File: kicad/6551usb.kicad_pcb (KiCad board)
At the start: 2 copper layers, 98.6 x 139.7 mm, 42 parts, among them J1 Conn_01x03_Male, P1 DLP-USB245R, SW1 SW_DIP_x06, U1 74LS04, U10 74LS74, U11 74LS86, U12 74LS33, U13 74LS273, U14 74LS374, U15 74LS244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

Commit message: Update to 1.01
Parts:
- U7: value 74LS09 -> 74LS08; footprint Package_DIP:DIP-20_W7.62mm -> Package_DIP:DIP-14_W7.62mm
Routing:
- net /D4: track 257.1 -> 203.1 mm, vias 2 -> 1
- net GND: track 700.5 -> 647.5 mm, vias 0 -> 1
- net /D0: track 244.6 -> 191.7 mm, vias 1 -> 2
- net /D6: track 250.3 -> 201.3 mm, vias 1 -> 2
- net /BUF_WRITE: track 118.3 -> 79.4 mm, vias 0 -> 1
- net /D3: track 231.2 -> 265.6 mm, vias 2 -> 1
- net /A6: track 136.1 -> 102.5 mm
- net /DELTA_PWREN*: track 66.9 -> 92.2 mm, vias 1 -> 0
- net /CD1: track 98.4 -> 79.2 mm, vias 1 -> 0
- net /COMMAND_SELECT: track 61.2 -> 42.6 mm
- net /D1: track 201.5 -> 219.5 mm, vias 2 -> 1
- net +5V: track 467.3 -> 451.8 mm
- net /A7: track 141.3 -> 125.9 mm, vias 0 -> 1
- net /CONTROL_SELECT: track 78.7 -> 63.4 mm
- net /A0: track 113.8 -> 99.9 mm
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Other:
- board text added: "USB Serial Pak for Color Computer v1.01 Copyright 2022 Don Barber License GPLv3 https://github.com/barberd/cocousbserial"
- board text removed: "USB Serial Pak for Color Computer v1.0 Copyright 2022 Don Barber License GPLv3 https://github.com/barberd/cocousbserial"

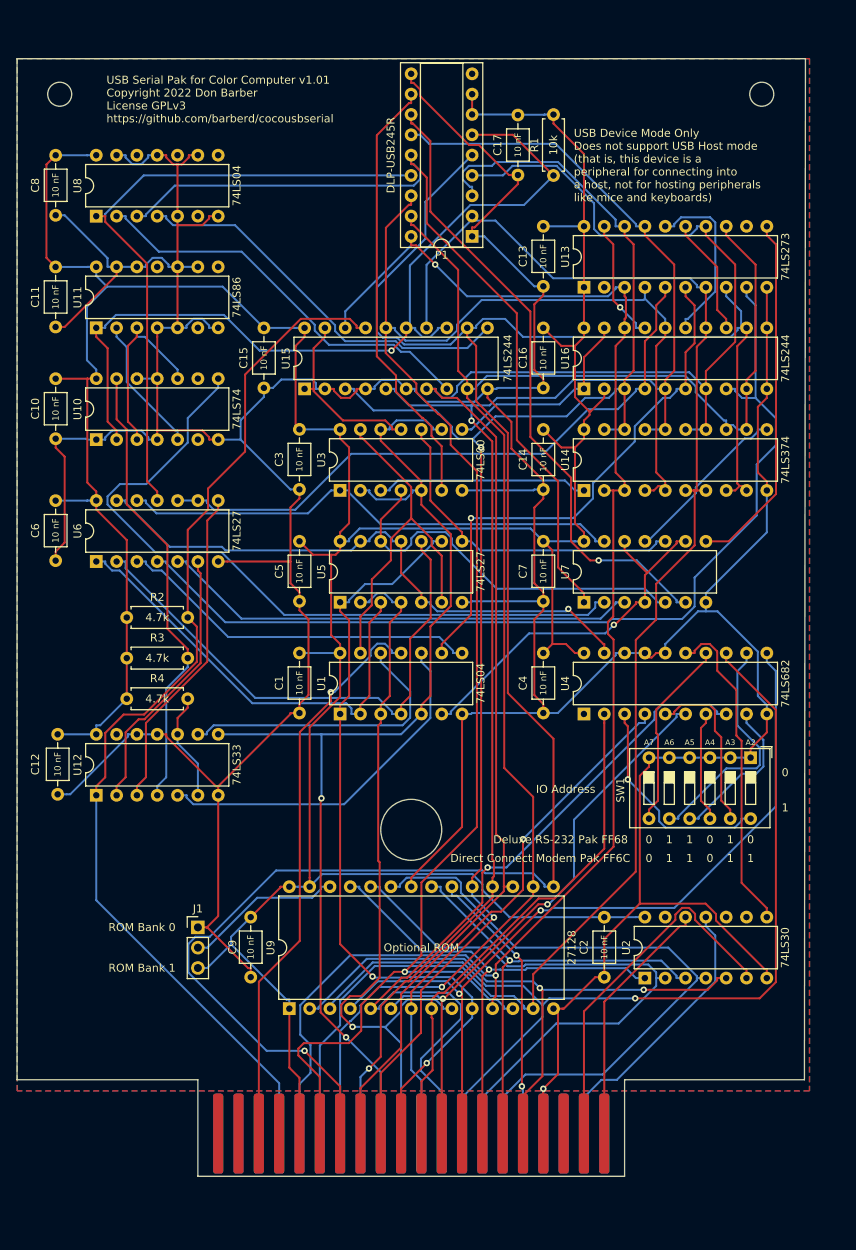
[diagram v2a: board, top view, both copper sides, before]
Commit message: Updated to 1.02 to fix E line
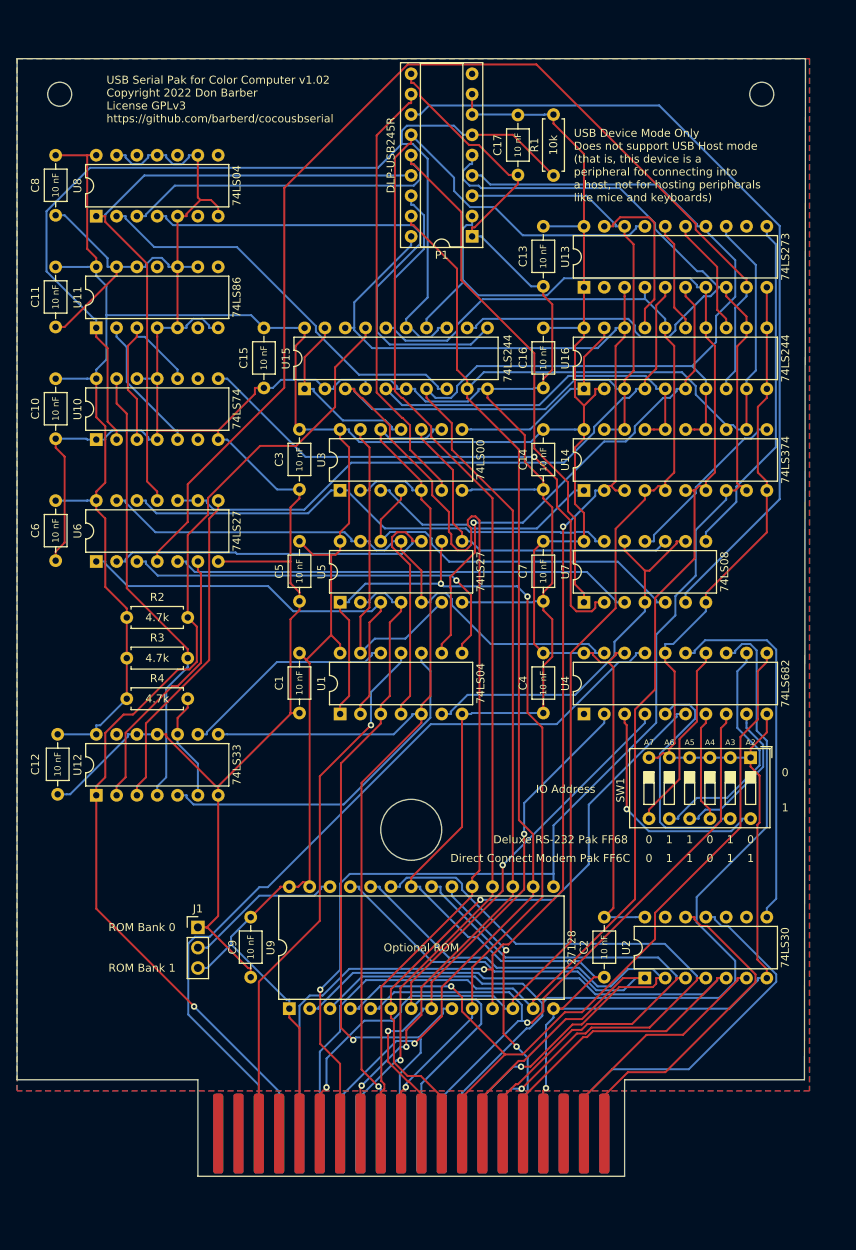
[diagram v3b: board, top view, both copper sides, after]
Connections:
- net /BOARD_SELECT renamed /BOARD_SELECT*
- U17 pad 6: unconnected-(U17-Pad6) -> /E
- U4 pad 17: GND -> /E
- U4 pad 18: GND -> +5V
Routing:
- net /E: track 0.00 -> 99.7 mm
- net /D3: track 265.6 -> 227.9 mm
- net /PWREN*: track 107.2 -> 136.3 mm, vias 1 -> 0
- net /D1: track 219.5 -> 194.0 mm
- net /BUF_WRITE: track 79.4 -> 104.7 mm, vias 1 -> 0
- net /DELTA_PWREN*: track 92.2 -> 69.4 mm, vias 0 -> 1
- net /CD3: track 121.2 -> 143.8 mm
- net /A0: track 99.9 -> 120.7 mm, vias 2 -> 3
- net /D6: track 201.3 -> 221.0 mm, vias 2 -> 1
- net /A12: track 76.5 -> 92.4 mm, vias 2 -> 0
- net /A13: track 46.1 -> 31.2 mm
- net GND: track 647.5 -> 662.4 mm
- net Net-(U15-Pad11): track 49.8 -> 63.9 mm
- net /A14: track 35.5 -> 47.4 mm
- net /A10: track 59.1 -> 70.8 mm, vias 1 -> 0
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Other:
- board text added: "USB Serial Pak for Color Computer v1.02 Copyright 2022 Don Barber License GPLv3 https://github.com/barberd/cocousbserial"
- board text removed: "USB Serial Pak for Color Computer v1.01 Copyright 2022 Don Barber License GPLv3 https://github.com/barberd/cocousbserial"

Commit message: Updated to 1.03 to fix interrupt in status register and extend board to full size
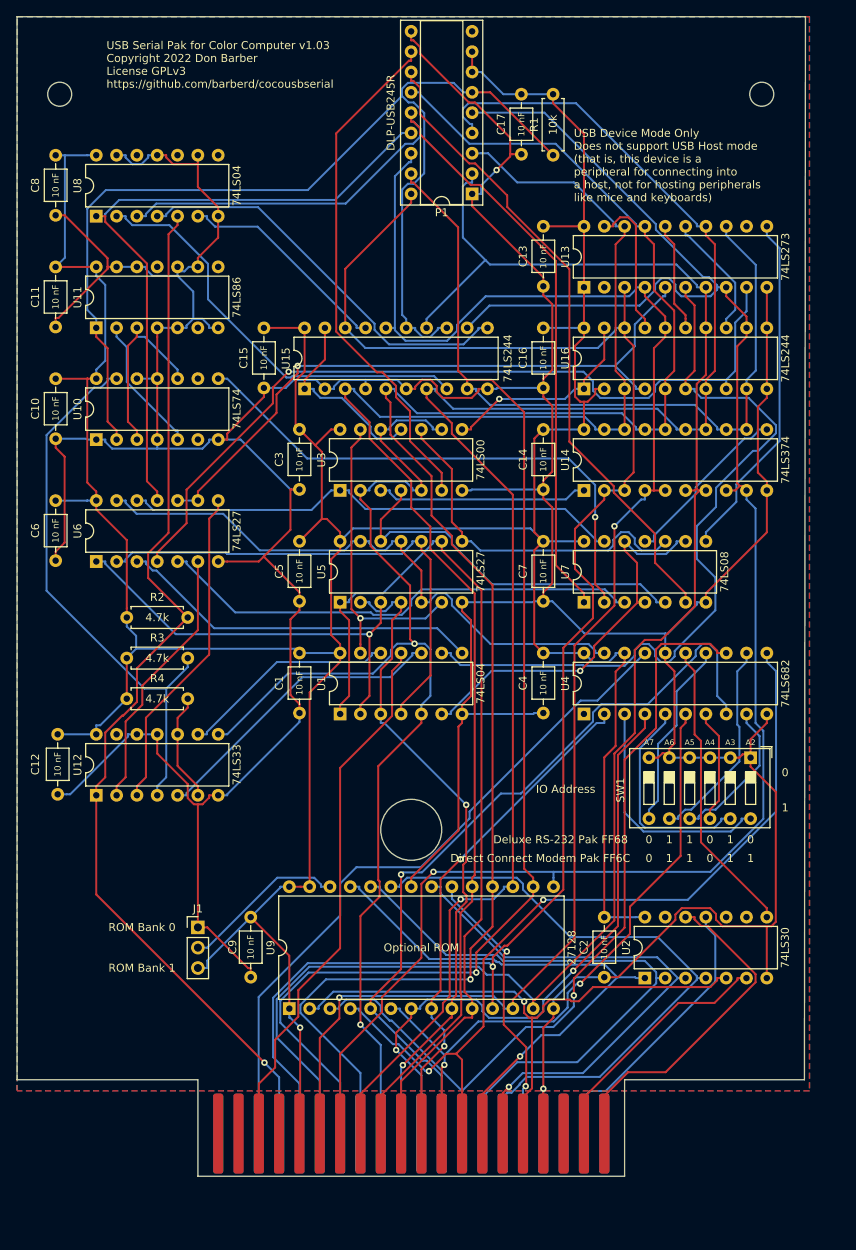
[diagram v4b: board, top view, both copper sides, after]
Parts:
- moved P1 5.31 mm to (69.8, 72.2)
- moved C17 2.64 mm to (76.0, 59.7)
- moved R1 2.54 mm to (80.0, 67.3)
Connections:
- U15 pad 17: /CART* -> /CART
- U8 pad 5: GND -> /CART*
- U8 pad 6: unconnected-(U8-Pad6) -> /CART
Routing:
- net /CD3: track 143.8 -> 102.4 mm, vias 0 -> 1
- net /CD2: track 65.8 -> 96.5 mm, vias 1 -> 0
- net /CART: track 0.00 -> 27.1 mm
- net /BUF_WRITE: track 104.7 -> 81.1 mm
- net /A7: track 127.8 -> 104.5 mm, vias 0 -> 1
- net /D4: track 200.3 -> 222.6 mm
- net /A12: track 92.4 -> 73.0 mm, vias 0 -> 1
- net /D2: track 195.6 -> 212.2 mm
- net /E: track 99.7 -> 86.0 mm
- net Net-(U15-Pad11): track 63.9 -> 50.4 mm
- net Net-(R3-Pad2): track 57.3 -> 70.1 mm
- net /D7: track 203.8 -> 191.4 mm
- net /D0: track 194.4 -> 206.6 mm, vias 2 -> 1
- net /A14: track 47.4 -> 35.5 mm
- net GND: track 662.4 -> 650.5 mm, vias 1 -> 2
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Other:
- board size 98.6 x 139.7 mm -> 98.6 x 144.9 mm
- board text added: "USB Serial Pak for Color Computer v1.03 Copyright 2022 Don Barber License GPLv3 https://github.com/barberd/cocousbserial"
- board text removed: "USB Serial Pak for Color Computer v1.02 Copyright 2022 Don Barber License GPLv3 https://github.com/barberd/cocousbserial"

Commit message: fixed fab files in kicad folder
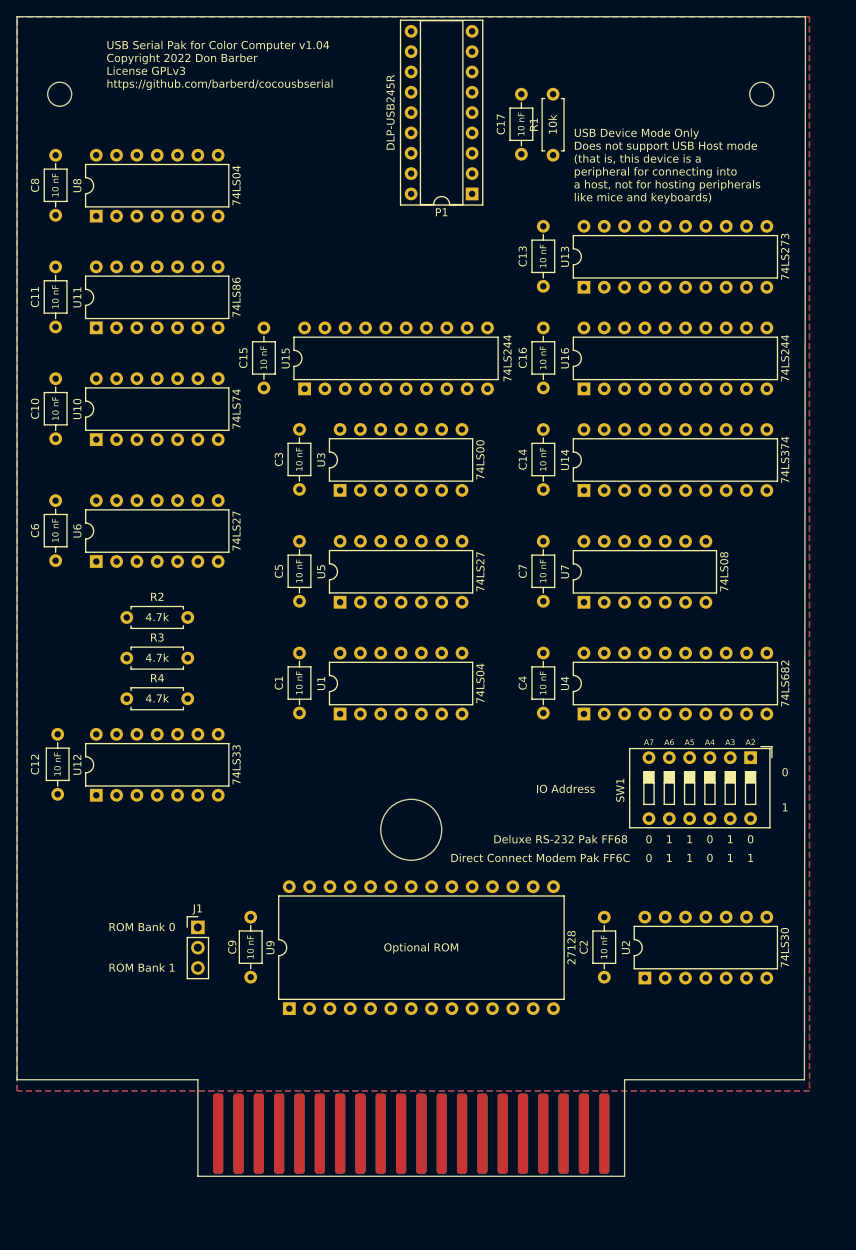
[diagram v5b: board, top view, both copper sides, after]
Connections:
- U10 pad 1: GND -> +5V
- U10 pad 4: GND -> +5V
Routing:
- net GND: track 650.5 -> 0.00 mm, vias 2 -> 0
- net +5V: track 455.9 -> 0.00 mm, vias 1 -> 0
- net /D3: track 232.7 -> 0.00 mm, vias 1 -> 0
- net /D6: track 223.5 -> 0.00 mm, vias 1 -> 0
- net /D4: track 222.6 -> 0.00 mm, vias 1 -> 0
- net /D5: track 213.0 -> 0.00 mm, vias 1 -> 0
- net /D2: track 212.2 -> 0.00 mm
- net /D0: track 206.6 -> 0.00 mm, vias 1 -> 0
- net /D1: track 201.5 -> 0.00 mm, vias 2 -> 0
- net /D7: track 191.4 -> 0.00 mm
- net /R/W*: track 146.7 -> 0.00 mm, vias 2 -> 0
- net /PWREN*: track 138.0 -> 0.00 mm
- net /CART*: track 132.5 -> 0.00 mm, vias 1 -> 0
- net /TXE*: track 114.3 -> 0.00 mm
- net /A0: track 112.7 -> 0.00 mm
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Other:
- board text added: "USB Serial Pak for Color Computer v1.04 Copyright 2022 Don Barber License GPLv3 https://github.com/barberd/cocousbserial"
- board text removed: "USB Serial Pak for Color Computer v1.03 Copyright 2022 Don Barber License GPLv3 https://github.com/barberd/cocousbserial"

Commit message: Updated to 1.04 to fix PWREN flipflop set and reset
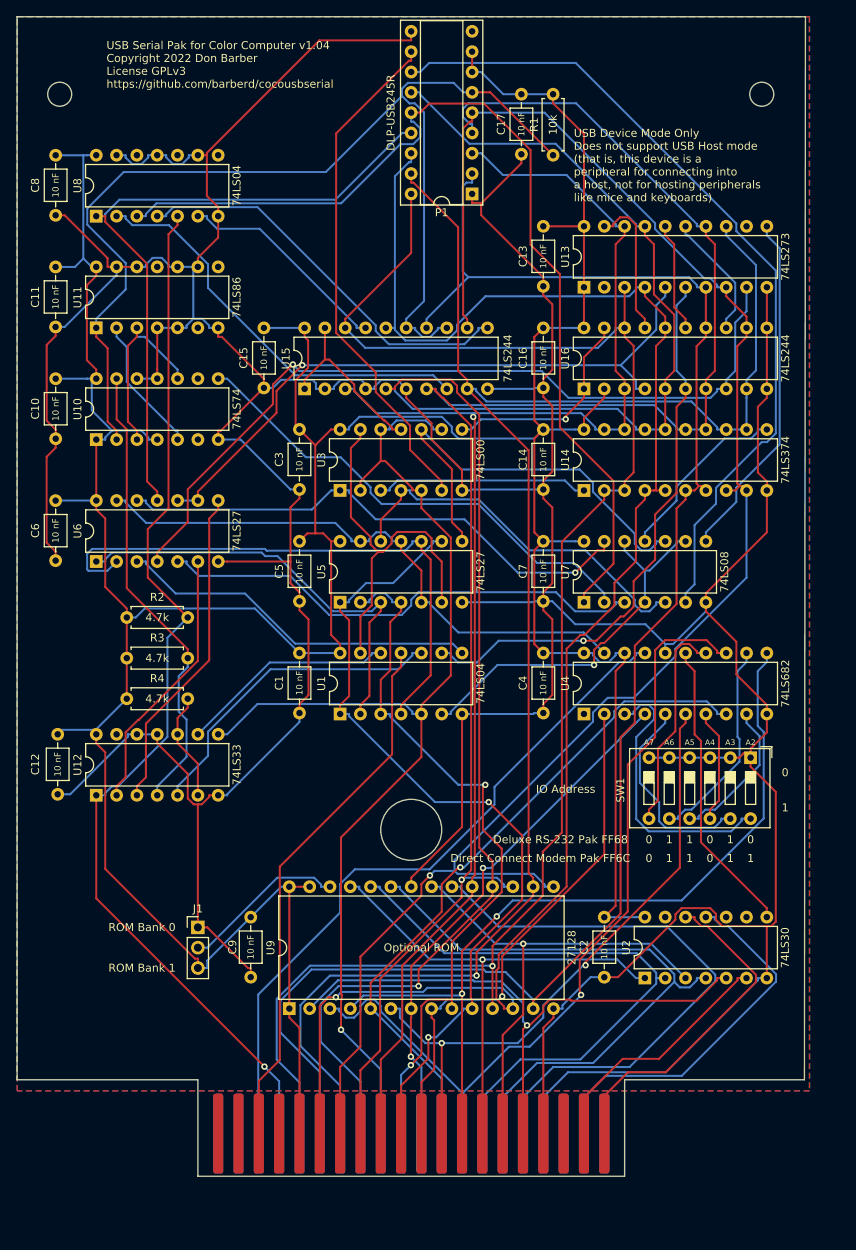
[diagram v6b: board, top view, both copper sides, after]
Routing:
- net GND: track 0.00 -> 697.7 mm
- net +5V: track 0.00 -> 475.0 mm
- net /D6: track 0.00 -> 223.2 mm, vias 0 -> 1
- net /D3: track 0.00 -> 217.1 mm, vias 0 -> 1
- net /D4: track 0.00 -> 216.1 mm, vias 0 -> 1
- net /D5: track 0.00 -> 213.5 mm, vias 0 -> 1
- net /D2: track 0.00 -> 209.1 mm
- net /D1: track 0.00 -> 206.0 mm, vias 0 -> 1
- net /D0: track 0.00 -> 203.5 mm, vias 0 -> 1
- net /D7: track 0.00 -> 181.7 mm, vias 0 -> 1
- net /R/W*: track 0.00 -> 141.7 mm, vias 0 -> 1
- net /PWREN*: track 0.00 -> 140.2 mm
- net /CART*: track 0.00 -> 133.6 mm, vias 0 -> 1
- net /TXE*: track 0.00 -> 123.5 mm
- net /A7: track 0.00 -> 106.1 mm, vias 0 -> 1
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
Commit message: Updated for correct logic on PWREN second flipflop
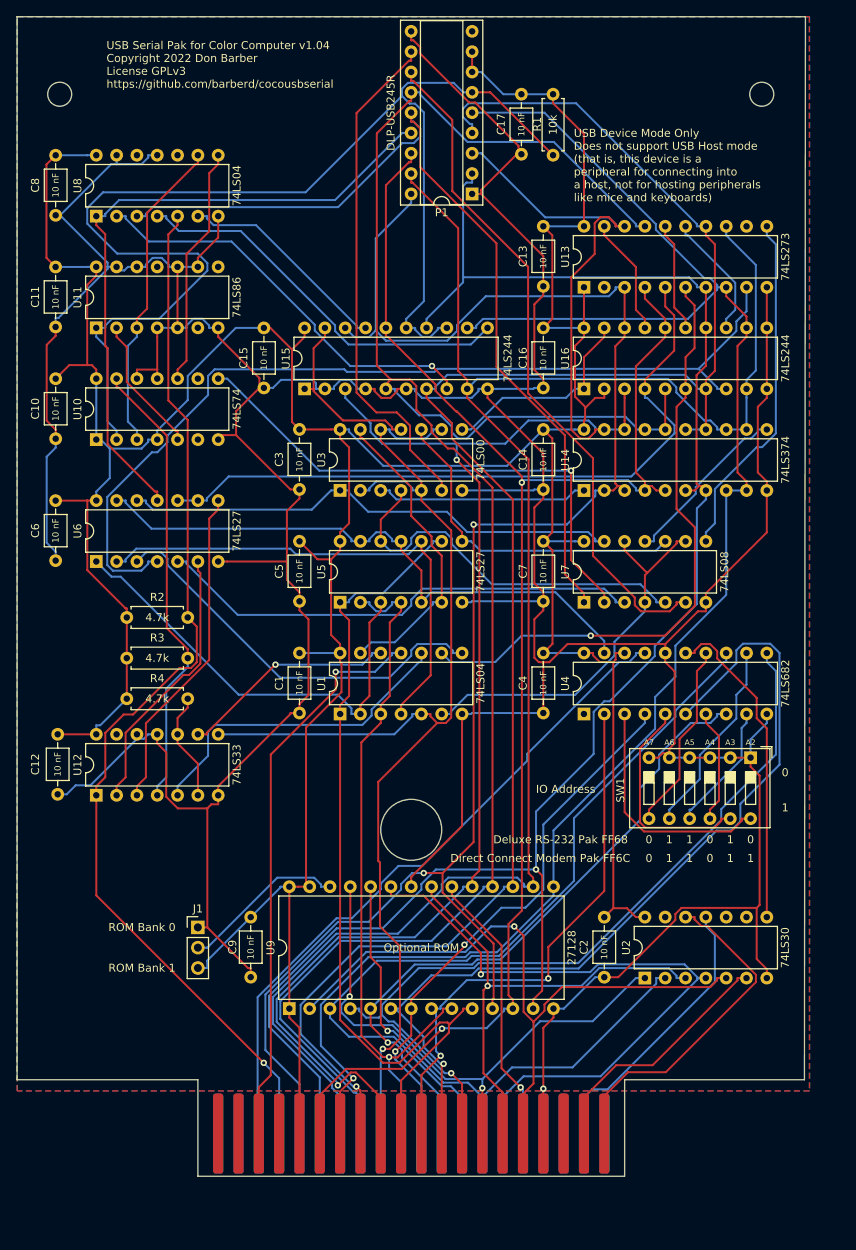
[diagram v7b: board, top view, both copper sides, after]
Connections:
- U10 pad 3: Net-(U10-Pad10) -> Net-(U10-Pad3)
- U11 pad 3: Net-(U10-Pad10) -> Net-(U10-Pad3)
- U8 pad 8: unconnected-(U8-Pad8) -> Net-(U10-Pad10)
- U8 pad 9: GND -> Net-(U10-Pad3)
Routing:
- net GND: track 697.7 -> 639.1 mm, vias 0 -> 1
- net Net-(U10-Pad3): track 0.00 -> 39.8 mm
- net /CTS*: track 73.1 -> 34.5 mm, vias 0 -> 1
- net /D7: track 181.7 -> 219.1 mm, vias 1 -> 2
- net /A4: track 79.6 -> 111.9 mm, vias 2 -> 1
- net /D6: track 223.2 -> 245.5 mm, vias 1 -> 0
- net /PWREN*: track 140.2 -> 158.7 mm
- net /BUF_WRITE: track 103.9 -> 85.7 mm
- net /D0: track 203.5 -> 218.6 mm, vias 1 -> 2
- net /CD3: track 101.9 -> 115.7 mm, vias 1 -> 0
- net /COMMAND_SELECT: track 54.9 -> 42.5 mm
- net /A14: track 47.4 -> 35.4 mm
- net /D5: track 213.5 -> 225.4 mm
- net /A12: track 74.1 -> 84.2 mm
- net /TXE*: track 123.5 -> 113.6 mm
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
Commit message: Added board 'wings' and moved chips around to make board prettier.
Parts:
- moved C15 43.9 mm to (78.7, 115.5)
- moved U15 43.9 mm to (83.8, 123.1)
- moved C7 40.7 mm to (48.1, 88.8)
- moved U7 40.7 mm to (53.2, 96.4)
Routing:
- net /D6: track 245.5 -> 173.3 mm, vias 0 -> 1
- net /D7: track 219.1 -> 153.1 mm, vias 2 -> 0
- net /CART: track 27.1 -> 89.2 mm, vias 0 -> 1
- net Net-(U15-Pad8): track 51.5 -> 104.3 mm, vias 1 -> 0
- net Net-(U15-Pad11): track 49.4 -> 100.2 mm
- net /D5: track 225.4 -> 176.3 mm
- net /CTS*: track 34.5 -> 83.0 mm, vias 1 -> 0
- net /DELTA_PWREN*: track 67.1 -> 18.7 mm, vias 1 -> 0
- net /E: track 84.4 -> 131.7 mm
- net /BUF_WRITE: track 85.7 -> 41.2 mm
- net GND: track 639.1 -> 683.0 mm, vias 1 -> 0
- net /TXE*: track 113.6 -> 74.6 mm
- net /D2: track 216.8 -> 183.8 mm, vias 1 -> 0
- net /A4: track 111.9 -> 79.6 mm, vias 1 -> 2
- net /CONTROL_WRITE: track 22.1 -> 51.9 mm
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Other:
- board size 98.6 x 144.9 mm -> 98.6 x 151.8 mm
- board text added: "USB Serial Pak for Color Computer v1.05 Copyright 2022 Don Barber License GPLv3 https://github.com/barberd/cocousbserial"
- board text removed: "USB Serial Pak for Color Computer v1.04 Copyright 2022 Don Barber License GPLv3 https://github.com/barberd/cocousbserial"
